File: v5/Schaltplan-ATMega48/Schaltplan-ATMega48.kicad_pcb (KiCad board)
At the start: 2 copper layers, 99.1 x 78.7 mm, 18 parts, among them J1 AVR-ISP-6, SW1 SW_Push, SW2 SW_Push, SW3 SW_Push, U1 ATmega48A-P, Y1 Crystal_Small

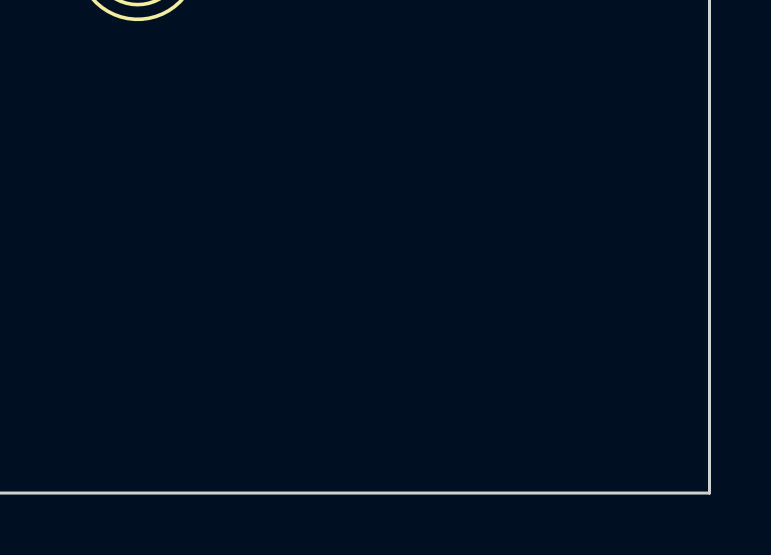
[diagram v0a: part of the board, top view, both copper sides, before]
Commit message: Add Tristans Matrikelnummer - can easily be changed to Hans one as well
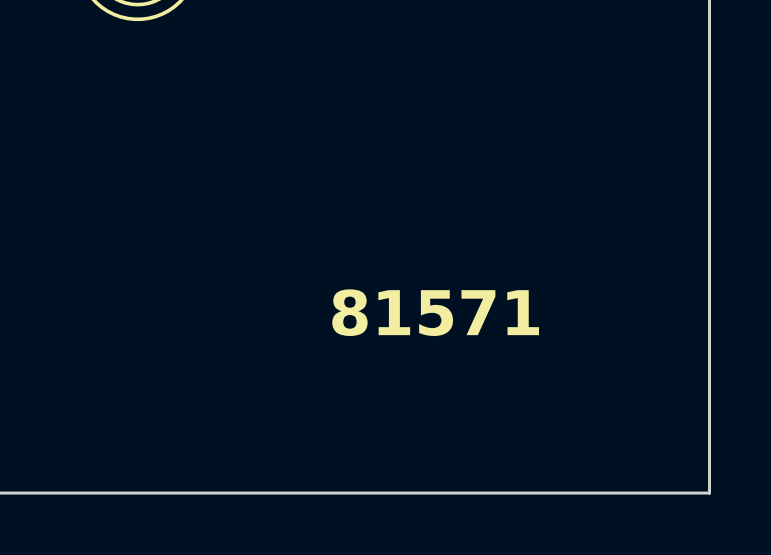
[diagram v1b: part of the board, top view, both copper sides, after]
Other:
- board text added: "81571"
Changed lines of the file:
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@@
   (gr_line (start 149.86 129.54) (end 50.8 129.54)
     (stroke (width 0.1) (type default)) (layer "Edge.Cuts"))
+  (gr_text "81571" (at 137.16 124.46) (layer "F.SilkS")
+    (effects (font (size 1.5 1.5) (thickness 0.3) bold) (justify left bottom))
+  )
   (segment (start 86.36 83.82) (end 86.36 101.6) (width 0.8) (layer "F.Cu") (net 1))
   (segment (start 107.636396 115.256396) (end 100.972792 121.92) (width 0.8) (layer "F.Cu") (net 1))

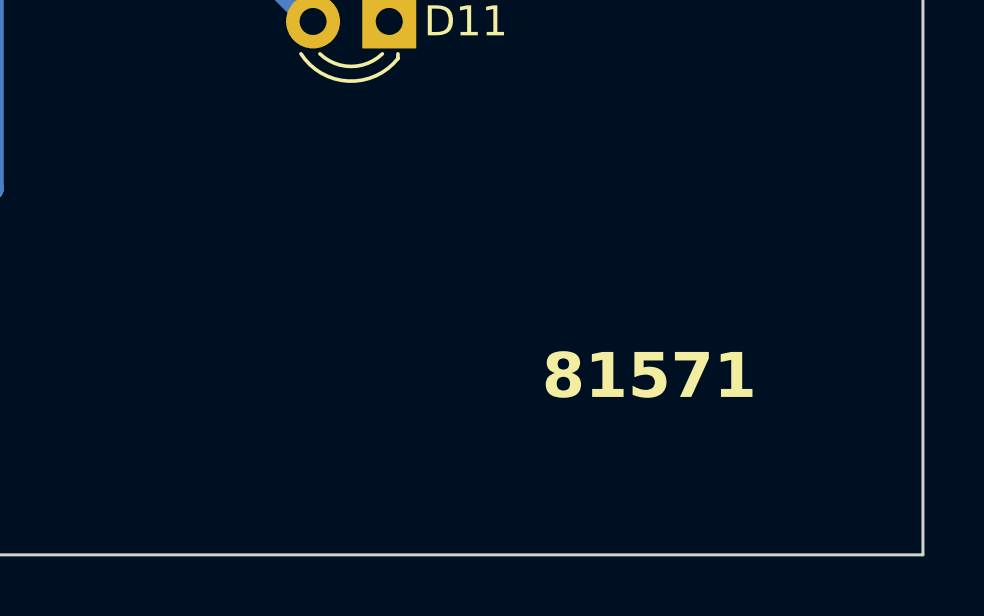
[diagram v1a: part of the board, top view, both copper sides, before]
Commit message: Increase font of Matrikelnummer
Add isolation around grounds as Ulbi said, gives warning that top copper layer is isolated
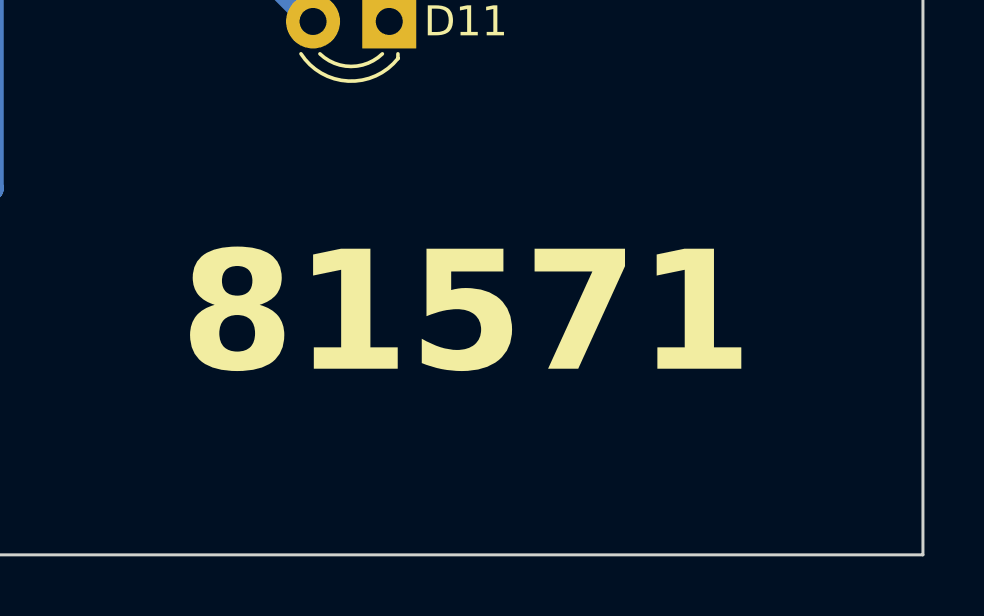
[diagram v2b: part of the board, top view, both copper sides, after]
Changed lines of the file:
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@@
   (gr_line (start 149.86 129.54) (end 50.8 129.54)
     (stroke (width 0.1) (type default)) (layer "Edge.Cuts"))
-  (gr_text "81571" (at 137.16 124.46) (layer "F.SilkS")
-    (effects (font (size 1.5 1.5) (thickness 0.3) bold) (justify left bottom))
+  (gr_text "81571" (at 125.095 123.825) (layer "F.SilkS")
+    (effects (font (size 4 4) (thickness 0.5) bold) (justify left bottom))
   )
   (segment (start 86.36 83.82) (end 86.36 101.6) (width 0.8) (layer "F.Cu") (net 1))
@@
   (segment (start 115.57 112.65) (end 114.68 111.76) (width 0.8) (layer "B.Cu") (net 27))
   (segment (start 115.57 114.3) (end 115.57 112.65) (width 0.8) (layer "B.Cu") (net 27))
+  (zone (net 0) (net_name "") (layer "F.Cu") (hatch edge 0.5)
+    (connect_pads (clearance 0))
+    (min_thickness 0.25) (filled_areas_thickness no)
+    (keepout (tracks not_allowed) (vias allowed) (pads allowed) (copperpour not_allowed) (footprints allowed))
+    (fill (thermal_gap 0.5) (thermal_bridge_width 0.5))
+    (polygon
+      (pts
+        (xy 130.175 84.455)
+        (xy 133.985 84.455)
+        (xy 133.985 113.665)
+        (xy 130.175 113.665)
+      )
+    )
+  )
   (zone (net 2) (net_name "GNDREF") (layer "F.Cu") (hatch edge 0.5)
     (connect_pads (clearance 0.5))
@@
       )
     )
+  )
+  (zone (net 0) (net_name "") (layer "F.Cu") (hatch edge 0.5)
+    (connect_pads (clearance 0))
+    (min_thickness 0.25) (filled_areas_thickness no)
+    (keepout (tracks not_allowed) (vias allowed) (pads allowed) (copperpour not_allowed) (footprints allowed))
+    (fill (thermal_gap 0.5) (thermal_bridge_width 0.5))
+    (polygon
+      (pts
+        (xy 98.425 99.695)
+        (xy 102.235 99.695)
+        (xy 102.235 103.505)
+        (xy 98.425 103.505)
+      )
+    )
+  )
+  (zone (net 0) (net_name "") (layer "F.Cu") (hatch edge 0.5)
+    (connect_pads (clearance 0))
+    (min_thickness 0.25) (filled_areas_thickness no)
+    (keepout (tracks not_allowed) (vias allowed) (pads allowed) (copperpour not_allowed) (footprints allowed))
+    (fill (thermal_gap 0.5) (thermal_bridge_width 0.5))
+    (polygon
+      (pts
+        (xy 66.675 112.395)
+        (xy 70.485 112.395)
+        (xy 70.485 126.365)
+        (xy 66.675 126.365)
+      )
+    )
+  )
+  (zone (net 0) (net_name "") (layer "F.Cu") (hatch edge 0.5)
+    (connect_pads (clearance 0))
+    (min_thickness 0.25) (filled_areas_thickness no)
+    (keepout (tracks not_allowed) (vias allowed) (pads allowed) (copperpour not_allowed) (footprints allowed))
+    (fill (thermal_gap 0.5) (thermal_bridge_width 0.5))
+    (polygon
+      (pts
+        (xy 108.585 63.5)
+        (xy 113.665 63.5)
+        (xy 113.665 68.58)
+        (xy 108.585 68.58)
+      )
+    )
+  )
+  (zone (net 0) (net_name "") (layer "F.Cu") (hatch edge 0.5)
+    (connect_pads (clearance 0))
+    (min_thickness 0.25) (filled_areas_thickness no)
+    (keepout (tracks not_allowed) (vias allowed) (pads allowed) (copperpour not_allowed) (footprints allowed))
+    (fill (thermal_gap 0.5) (thermal_bridge_width 0.5))
+    (polygon
+      (pts
+        (xy 90.805 102.235)
+        (xy 94.615 102.235)
+        (xy 94.615 106.045)
+        (xy 90.805 106.045)
+      )
+    )
+  )
+  (zone (net 0) (net_name "") (layer "F.Cu") (hatch edge 0.5)
+    (connect_pads (clearance 0))
+    (min_thickness 0.25) (filled_areas_thickness no)
+    (keepout (tracks not_allowed) (vias allowed) (pads allowed) (copperpour not_allowed) (footprints allowed))
+    (fill (thermal_gap 0.5) (thermal_bridge_width 0.5))
+    (polygon
+      (pts
+        (xy 111.125 117.475)
+        (xy 114.935 117.475)
+        (xy 114.935 121.285)
+        (xy 111.125 121.285)
+      )
+    )
+  )
+  (zone (net 0) (net_name "") (layer "F.Cu") (hatch edge 0.5)
+    (connect_pads (clearance 0))
+    (min_thickness 0.25) (filled_areas_thickness no)
+    (keepout (tracks not_allowed) (vias allowed) (pads allowed) (copperpour not_allowed) (footprints allowed))
+    (fill (thermal_gap 0.5) (thermal_bridge_width 0.5))
+    (polygon
+      (pts
+        (xy 66.675 76.835)
+        (xy 71.12 76.835)
+        (xy 71.12 104.775)
+        (xy 66.675 104.775)
+      )
+    )
